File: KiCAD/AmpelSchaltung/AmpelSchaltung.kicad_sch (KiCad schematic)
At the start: 14 parts, among them SW1 SW_DPDT_x2, SW2 SW_DPDT_x2, U1 74HC00, U2 74HC00, U3 AMS1117-3.3

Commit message: update pcb
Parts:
- added D5, D6, D7, D8: LED, symbol Device:LED
- added R5, R6, R7, R8: 1k, symbol Device:R
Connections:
- net GND: now also D5.1 (K), D6.1 (K), D7.1 (K), D8.1 (K)
- net at R1.1, U1.6: now also R5.1
- net at R4.1, U1.11: now also R8.1
- net at R2.1, U1.3, U1.4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: now also R6.1
- net at R3.1, U1.8: now also R7.1
- new net: D6.2 (A), R6.2
- new net: D8.2 (A), R8.2
- new net: D7.2 (A), R7.2
- new net: D5.2 (A), R5.2
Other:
- moved on the sheet: D1, D2, D3, D4, R1, R2, R3, R4, RV1, SW1A, SW2A, U1A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

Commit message: added ampelschaltung PCB
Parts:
- removed SW1, SW2: SW_DPDT_x2, symbol Switch:SW_DPDT_x2
- added H1, H2, H3, H4: MountingHole, MountingHole:MountingHole_3.2mm_M3, symbol Mechanical:MountingHole
- added J1: PWR, TerminalBlock_MetzConnect:TerminalBlock_MetzConnect_Type055_RT01502HDWU_1x02_P5.00mm_Horizontal, symbol Connector:Screw_Terminal_01x02
- added J2: usb, Connector_PinHeader_2.54mm:PinHeader_1x05_P2.54mm_Vertical, symbol Connector:Conn_01x05_Pin
- added J3: Conn_01x06_Pin, Connector_PinHeader_2.54mm:PinHeader_1x06_P2.54mm_Vertical, symbol Connector:Conn_01x06_Pin
- added J5: Conn_01x04_Pin, Connector_PinHeader_2.54mm:PinHeader_1x04_P2.54mm_Vertical, symbol Connector:Conn_01x04_Pin
- added J6: Conn_01x08_Pin, Connector_PinHeader_2.54mm:PinHeader_1x08_P2.54mm_Vertical, symbol Connector:Conn_01x08_Pin
- added SW3, SW4: SW_SPDT, Library:Goobay10020, symbol Switch:SW_SPDT
- D1, D2, D3, D4, D5, D6, D7, D8: footprint (none) -> LED_THT:LED_D5.0mm_Clear
- R1, R2, R3, R4, R5, R6, R7, R8: footprint (none) -> Resistor_SMD:R_0805_2012Metric_Pad1.20x1.40mm_HandSolder
- RV1: footprint (none) -> Potentiometer_THT:Potentiometer_Alpha_RD901F-40-00D_Single_Vertical
- U1, U2: footprint (none) -> Package_DIP:DIP-14_W7.62mm_Socket
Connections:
- net +5V: now also J1.1 (Pin_1), J2.5 (Pin_5), J3.4 (Pin_4), J3.5 (Pin_5), J3.6 (Pin_6), SW3.1 (A)
- net GND: now also J1.2 (Pin_2), J2.1 (Pin_1), J3.1 (Pin_1), J3.2 (Pin_2), J3.3 (Pin_3), J5.3 (Pin_3), J5.4 (Pin_4), SW3.3 (C)
- net at D2.2 (A): now also R2.1; no longer R2.2
- net at D3.2 (A): now also R3.1; no longer R3.2
- net at U1.3, U1.4, U1.5: now also R2.2, R6.2, J6.5 (Pin_5), J6.6 (Pin_6); no longer R2.1, R6.1
- net at D6.2 (A): now also R6.1; no longer R6.2
- net at R1.1, U1.6: now also R5.2, J6.7 (Pin_7), J6.8 (Pin_8); no longer R5.1
- net at R8.2: now also R4.2, U1.11, J6.1 (Pin_1), J6.2 (Pin_2); no longer D8.2 (A)
- net at D7.2 (A): now also R7.1; no longer R7.2
- net at RV1.1: now also SW3.2 (B), SW4.1 (A)
- net at RV1.2: now also SW4.3 (C)
- net at D5.2 (A): now also R5.1; no longer R5.2
- net at U1.1, U1.2, U2.1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: now also J5.1 (Pin_1), J5.2 (Pin_2), SW4.2 (B)
- net at D4.2 (A): now also R4.1; no longer R4.2
- new net: D8.2 (A), R8.1
- new net: J6.3 (Pin_3), J6.4 (Pin_4), R3.2, R7.2, U1.8
- no-connect marks 2 -> 5
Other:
- note added: "GRUEN"
- note added: "ROT"
- moved on the sheet: R2, R3, R4, R5, R6, R7, R8

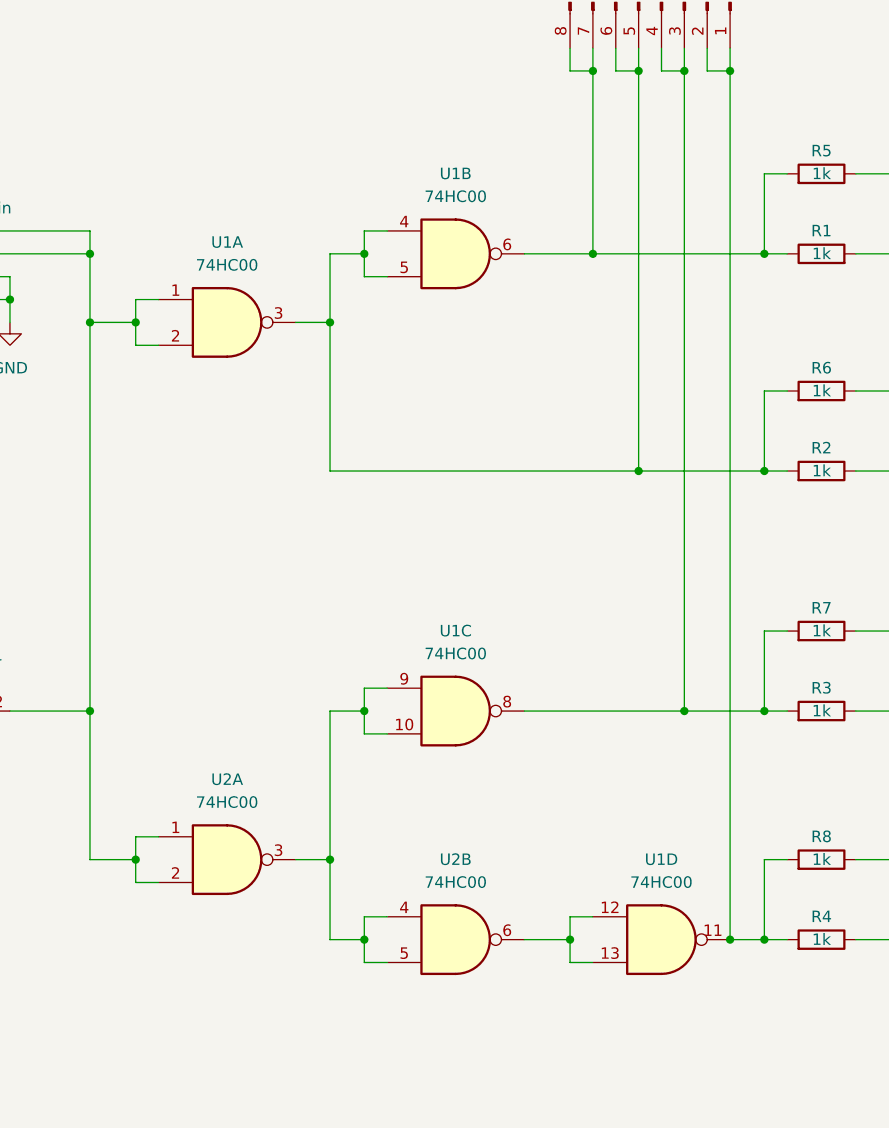
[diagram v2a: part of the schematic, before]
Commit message: routed ampelschaltung
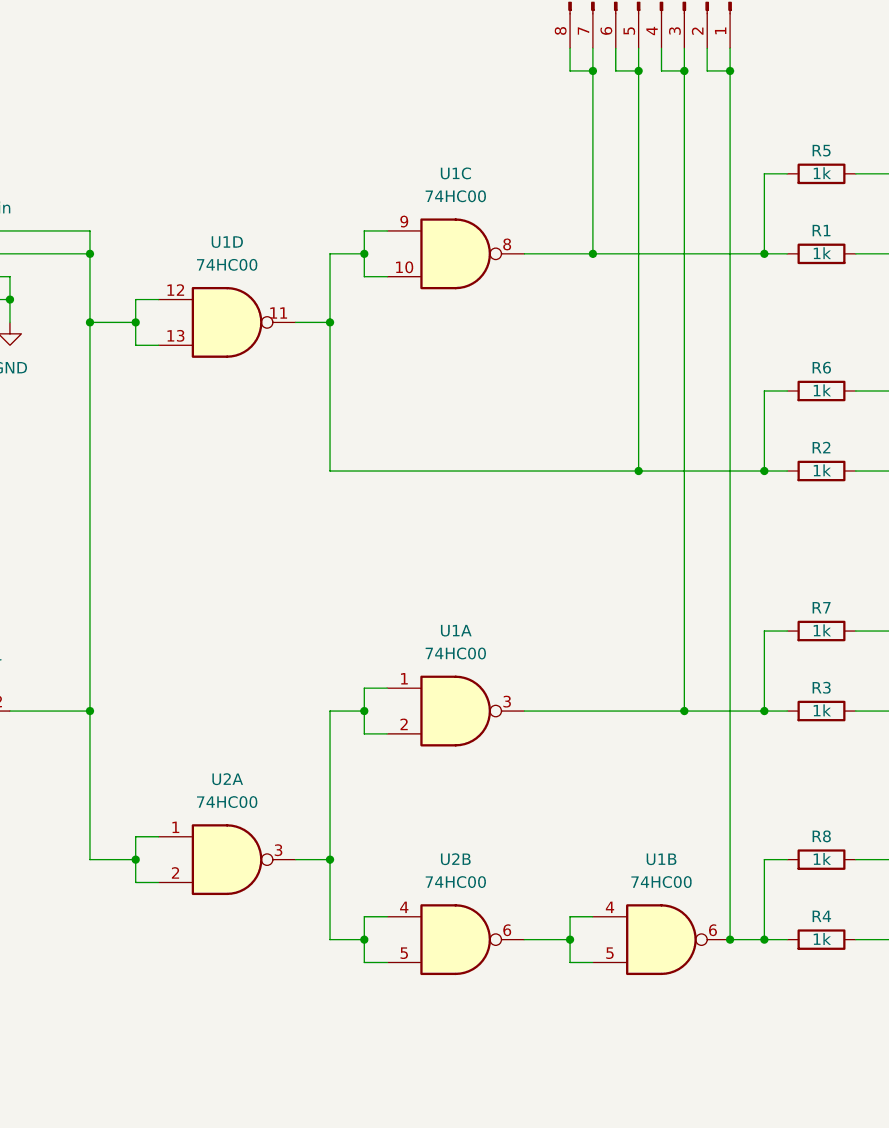
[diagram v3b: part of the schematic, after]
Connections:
- net at J5.1 (Pin_1), J5.2 (Pin_2), SW4.2 (B)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: now also U1.12, U1.13; no longer U1.1, U1.2
- net at J6.5 (Pin_5), J6.6 (Pin_6), R2.2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: now also U1.10, U1.11, U1.9; no longer U1.3, U1.4, U1.5
- net at J6.7 (Pin_7), J6.8 (Pin_8), R1.1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: now also U1.8; no longer U1.6
- net at J6.1 (Pin_1), J6.2 (Pin_2), R4.2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: now also U1.6; no longer U1.11
- net at J6.3 (Pin_3), J6.4 (Pin_4), R3.2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: now also U1.3; no longer U1.8
- net at U2.3, U2.4, U2.5: now also U1.1, U1.2; no longer U1.10, U1.9
- new net: U1.4, U1.5, U2.6
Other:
- moved on the sheet: U1A, U1B, U1C, U1D
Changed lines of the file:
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@@
   (junction (at 144.78 57.15) (diameter 0) (color 0 0 0 0)
   )
+  (junction (at 69.85 64.77) (diameter 0) (color 0 0 0 0)
+  )
+  (junction (at 69.85 57.15) (diameter 0) (color 0 0 0 0)
+  )
+  (junction (at 256.54 81.28) (diameter 0) (color 0 0 0 0)
+  )
+  (junction (at 100.33 133.35) (diameter 0) (color 0 0 0 0)
+  )
+  (junction (at 60.96 62.23) (diameter 0) (color 0 0 0 0)
+  )
+  (junction (at 170.18 72.39) (diameter 0) (color 0 0 0 0)
+  )
+  (junction (at 96.52 124.46) (diameter 0) (color 0 0 0 0)
+  )
+  (junction (at 74.93 124.46) (diameter 0) (color 0 0 0 0)
+  )
+  (junction (at 232.41 81.28) (diameter 0) (color 0 0 0 0)
+  )
+  (junction (at 130.81 81.28) (diameter 0) (color 0 0 0 0)
+  )
+  (junction (at 123.19 133.35) (diameter 0) (color 0 0 0 0)
+  )
+  (junction (at 201.93 132.08) (diameter 0) (color 0 0 0 0)
+  )
+  (junction (at 144.78 133.35) (diameter 0) (color 0 0 0 0)
+  )
+  (junction (at 140.97 36.83) (diameter 0) (color 0 0 0 0)
+  )
+  (junction (at 100.33 57.15) (diameter 0) (color 0 0 0 0)
+  )
+  (junction (at 170.18 99.06) (diameter 0) (color 0 0 0 0)
+  )
+  (junction (at 242.57 104.14) (diameter 0) (color 0 0 0 0)
+  )
+  (junction (at 135.89 107.95) (diameter 0) (color 0 0 0 0)
+  )
+  (junction (at 170.18 133.35) (diameter 0) (color 0 0 0 0)
+  )
+  (junction (at 170.18 107.95) (diameter 0) (color 0 0 0 0)
+  )
+  (junction (at 96.52 64.77) (diameter 0) (color 0 0 0 0)
+  )
+  (junction (at 125.73 36.83) (diameter 0) (color 0 0 0 0)
+  )
+  (junction (at 170.18 57.15) (diameter 0) (color 0 0 0 0)
+  )
+  (junction (at 201.93 129.54) (diameter 0) (color 0 0 0 0)
+  )
+  (junction (at 201.93 142.24) (diameter 0) (color 0 0 0 0)
+  )
+  (junction (at 144.78 107.95) (diameter 0) (color 0 0 0 0)
+  )
+  (junction (at 74.93 64.77) (diameter 0) (color 0 0 0 0)
+  )
+  (junction (at 144.78 81.28) (diameter 0) (color 0 0 0 0)
+  )
   (junction (at 140.97 133.35) (diameter 0) (color 0 0 0 0)
-  )
-  (junction (at 69.85 64.77) (diameter 0) (color 0 0 0 0)
-  )
-  (junction (at 69.85 57.15) (diameter 0) (color 0 0 0 0)
-  )
-  (junction (at 256.54 81.28) (diameter 0) (color 0 0 0 0)
-  )
-  (junction (at 100.33 133.35) (diameter 0) (color 0 0 0 0)
-  )
-  (junction (at 60.96 62.23) (diameter 0) (color 0 0 0 0)
-  )
-  (junction (at 170.18 72.39) (diameter 0) (color 0 0 0 0)
-  )
-  (junction (at 96.52 124.46) (diameter 0) (color 0 0 0 0)
-  )
-  (junction (at 74.93 124.46) (diameter 0) (color 0 0 0 0)
-  )
-  (junction (at 232.41 81.28) (diameter 0) (color 0 0 0 0)
-  )
-  (junction (at 130.81 81.28) (diameter 0) (color 0 0 0 0)
-  )
-  (junction (at 123.19 133.35) (diameter 0) (color 0 0 0 0)
-  )
-  (junction (at 201.93 132.08) (diameter 0) (color 0 0 0 0)
-  )
-  (junction (at 144.78 133.35) (diameter 0) (color 0 0 0 0)
-  )
-  (junction (at 140.97 36.83) (diameter 0) (color 0 0 0 0)
-  )
-  (junction (at 100.33 57.15) (diameter 0) (color 0 0 0 0)
-  )
-  (junction (at 170.18 99.06) (diameter 0) (color 0 0 0 0)
-  )
-  (junction (at 242.57 104.14) (diameter 0) (color 0 0 0 0)
-  )
-  (junction (at 135.89 107.95) (diameter 0) (color 0 0 0 0)
-  )
-  (junction (at 170.18 133.35) (diameter 0) (color 0 0 0 0)
-  )
-  (junction (at 170.18 107.95) (diameter 0) (color 0 0 0 0)
-  )
-  (junction (at 96.52 64.77) (diameter 0) (color 0 0 0 0)
-  )
-  (junction (at 125.73 36.83) (diameter 0) (color 0 0 0 0)
-  )
-  (junction (at 170.18 57.15) (diameter 0) (color 0 0 0 0)
-  )
-  (junction (at 201.93 129.54) (diameter 0) (color 0 0 0 0)
-  )
-  (junction (at 201.93 142.24) (diameter 0) (color 0 0 0 0)
-  )
-  (junction (at 144.78 107.95) (diameter 0) (color 0 0 0 0)
-  )
-  (junction (at 74.93 64.77) (diameter 0) (color 0 0 0 0)
-  )
-  (junction (at 144.78 81.28) (diameter 0) (color 0 0 0 0)
   )
   (junction (at 69.85 107.95) (diameter 0) (color 0 0 0 0)
@@
     )
   )
-  (symbol (lib_id "74xx:74HC00") (at 133.35 133.35 0) (unit 4)
-    (in_bom yes) (on_board yes) (dnp no) (fields_autoplaced)
-    (property "Reference" "U1" (at 133.3417 124.46 0)
-      (effects (font (size 1.27 1.27)))
-    )
-    (property "Value" "74HC00" (at 133.3417 127 0)
-      (effects (font (size 1.27 1.27)))
-    )
-    (property "Footprint" "Package_DIP:DIP-14_W7.62mm_Socket" (at 133.35 133.35 0)
-      (effects (font (size 1.27 1.27)) hide)
-    )
-    (property "Datasheet" "http://www.ti.com/lit/gpn/sn74hc00" (at 133.35 133.35 0)
+  (symbol (lib_id "74xx:74HC00") (at 85.09 64.77 0) (unit 4)
+    (in_bom yes) (on_board yes) (dnp no) (fields_autoplaced)
+    (property "Reference" "U1" (at 85.0817 55.88 0)
+      (effects (font (size 1.27 1.27)))
+    )
+    (property "Value" "74HC00" (at 85.0817 58.42 0)
+      (effects (font (size 1.27 1.27)))
+    )
+    (property "Footprint" "Package_DIP:DIP-14_W7.62mm_Socket" (at 85.09 64.77 0)
+      (effects (font (size 1.27 1.27)) hide)
+    )
+    (property "Datasheet" "http://www.ti.com/lit/gpn/sn74hc00" (at 85.09 64.77 0)
       (effects (font (size 1.27 1.27)) hide)
     )
@@
     )
   )
-  (symbol (lib_id "74xx:74HC00") (at 110.49 57.15 0) (unit 2)
-    (in_bom yes) (on_board yes) (dnp no) (fields_autoplaced)
-    (property "Reference" "U1" (at 110.4817 48.26 0)
-      (effects (font (size 1.27 1.27)))
-    )
-    (property "Value" "74HC00" (at 110.4817 50.8 0)
-      (effects (font (size 1.27 1.27)))
-    )
-    (property "Footprint" "Package_DIP:DIP-14_W7.62mm_Socket" (at 110.49 57.15 0)
-      (effects (font (size 1.27 1.27)) hide)
-    )
-    (property "Datasheet" "http://www.ti.com/lit/gpn/sn74hc00" (at 110.49 57.15 0)
+  (symbol (lib_id "74xx:74HC00") (at 133.35 133.35 0) (unit 2)
+    (in_bom yes) (on_board yes) (dnp no) (fields_autoplaced)
+    (property "Reference" "U1" (at 133.3417 124.46 0)
+      (effects (font (size 1.27 1.27)))
+    )
+    (property "Value" "74HC00" (at 133.3417 127 0)
+      (effects (font (size 1.27 1.27)))
+    )
+    (property "Footprint" "Package_DIP:DIP-14_W7.62mm_Socket" (at 133.35 133.35 0)
+      (effects (font (size 1.27 1.27)) hide)
+    )
+    (property "Datasheet" "http://www.ti.com/lit/gpn/sn74hc00" (at 133.35 133.35 0)
       (effects (font (size 1.27 1.27)) hide)
     )
@@
     )
   )
-  (symbol (lib_id "74xx:74HC00") (at 85.09 64.77 0) (unit 1)
-    (in_bom yes) (on_board yes) (dnp no) (fields_autoplaced)
-    (property "Reference" "U1" (at 85.0817 55.88 0)
-      (effects (font (size 1.27 1.27)))
-    )
-    (property "Value" "74HC00" (at 85.0817 58.42 0)
-      (effects (font (size 1.27 1.27)))
-    )
-    (property "Footprint" "Package_DIP:DIP-14_W7.62mm_Socket" (at 85.09 64.77 0)
-      (effects (font (size 1.27 1.27)) hide)
-    )
-    (property "Datasheet" "http://www.ti.com/lit/gpn/sn74hc00" (at 85.09 64.77 0)
+  (symbol (lib_id "74xx:74HC00") (at 110.49 107.95 0) (unit 1)
+    (in_bom yes) (on_board yes) (dnp no) (fields_autoplaced)
+    (property "Reference" "U1" (at 110.4817 99.06 0)
+      (effects (font (size 1.27 1.27)))
+    )
+    (property "Value" "74HC00" (at 110.4817 101.6 0)
+      (effects (font (size 1.27 1.27)))
+    )
+    (property "Footprint" "Package_DIP:DIP-14_W7.62mm_Socket" (at 110.49 107.95 0)
+      (effects (font (size 1.27 1.27)) hide)
+    )
+    (property "Datasheet" "http://www.ti.com/lit/gpn/sn74hc00" (at 110.49 107.95 0)
       (effects (font (size 1.27 1.27)) hide)
     )
@@
     )
   )
-  (symbol (lib_id "74xx:74HC00") (at 110.49 107.95 0) (unit 3)
-    (in_bom yes) (on_board yes) (dnp no) (fields_autoplaced)
-    (property "Reference" "U1" (at 110.4817 99.06 0)
-      (effects (font (size 1.27 1.27)))
-    )
-    (property "Value" "74HC00" (at 110.4817 101.6 0)
-      (effects (font (size 1.27 1.27)))
-    )
-    (property "Footprint" "Package_DIP:DIP-14_W7.62mm_Socket" (at 110.49 107.95 0)
-      (effects (font (size 1.27 1.27)) hide)
-    )
-    (property "Datasheet" "http://www.ti.com/lit/gpn/sn74hc00" (at 110.49 107.95 0)
-      (effects (font (size 1.27 1.27)) hide)
-    )
+  (symbol (lib_id "74xx:74HC00") (at 110.49 57.15 0) (unit 3)
+    (in_bom yes) (on_board yes) (dnp no) (fields_autoplaced)
+    (property "Reference" "U1" (at 110.4817 48.26 0)
+      (effects (font (size 1.27 1.27)))
+    )
+    (property "Value" "74HC00" (at 110.4817 50.8 0)
+      (effects (font (size 1.27 1.27)))
+    )
+    (property "Footprint" "Package_DIP:DIP-14_W7.62mm_Socket" (at 110.49 57.15 0)
+      (effects (font (size 1.27 1.27)) hide)
+    )
+    (property "Datasheet" "http://www.ti.com/lit/gpn/sn74hc00" (at 110.49 57.15 0)
+      (effects (font (size 1.27 1.27)) hide)
+    )

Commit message: added schematics
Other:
- title: (none) -> Ampelschaltung
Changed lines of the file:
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@@
 (kicad_sch (version 20230121) (generator eeschema)
   (paper "A4")
+  (title_block
+    (title "Ampelschaltung")
+    (comment 1 "Author: Alexander Hold")
+  )
   (junction (at 135.89 36.83) (diameter 0) (color 0 0 0 0)
   )
